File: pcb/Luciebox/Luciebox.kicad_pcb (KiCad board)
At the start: 2 copper layers, 100 x 100 mm, 91 parts, among them J1 Screw_Terminal_01x07, J2 Screw_Terminal_01x07, J3 Screw_Terminal_01x07, J4 Screw_Terminal_01x07, J5 Screw_Terminal_01x07, P1 CONN_01X01, P2 CONN_01X01, P3 CONN_01X01, P4 CONN_01X01, P5 Digital, P6 Power, P7 Digital, P8 Analog, Q1 BC558, Q2 N-Channel_Mosfet, T1 terminal_13x1, T10 terminal_8x1, T11 terminal_3x1, T2 terminal_8x1, T3 terminal_8x1, T4 terminal_8x1, T5 terminal_8x1, T6 terminal_8x1, T7 terminal_8x1, T8 terminal_8x1, T9 terminal_8x1, U1 CA56-12SRWA, U2 ULN2003A, U3 ATmega328-PU, Y1 16MHz

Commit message: fiddling with traces
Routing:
- net /0(Rx): track 149.7 -> 136.9 mm
- net /3(PWM): track 132.3 -> 142.8 mm
- net /2: track 110.3 -> 113.2 mm
- net /11(PWM-MOSI): track 72.4 -> 70.1 mm
- net /13(SCK): track 113.9 -> 115.5 mm
- net /1(Tx): track 77.6 -> 76.8 mm
- net /12(MISO): track 146.0 -> 145.2 mm

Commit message: pcb v1.0.0 looks like all done!
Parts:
- added G***: LOGO, artwork:titles_and_text, F.Cu at (54.6, 44.8)
- added G***: LOGO, artwork:sky_with_clouds_negative, F.Cu at (50.3, 49.9)
- added U4: 8X8PADS, Luciebox:64_PADS_100mil, F.Cu at (89.5, 43.5)
- moved H6 124.7 mm to (21.1, 27.1)
- moved H5 122.3 mm to (17.9, 61.2)
- moved H7 110.3 mm to (20.7, 69.4)
- moved J4 53.3 mm to (62.0, 3.92), turned to 180 degrees
- moved H8 38.3 mm to (94.1, 77.1)
- moved Q2 28.2 mm to (32.0, 18.2)
- moved R48 27.6 mm to (35.5, 14.4)
- moved R47 22.8 mm to (35.5, 11.8), turned to 180 degrees
- moved R19 18.5 mm to (75.2, 56.0), turned to 180 degrees
- moved Q1 6.78 mm to (37.1, 3.70)
- moved R1 5.04 mm to (35.5, 9.03), turned to 180 degrees
- moved R5 4.19 mm to (43.2, 30.4), turned to 90 degrees
- moved R4 1.79 mm to (53.1, 30.3)
- moved R3 0.42 mm to (57.9, 30.3)
- moved T11 0.27 mm to (2.28, 46.1)
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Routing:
- net VCC: track 293.5 -> 364.0 mm, vias 2 -> 1
- net Net-(J5-Pad2): track 24.7 -> 56.3 mm
- net /1(Tx): track 76.8 -> 104.2 mm, vias 0 -> 1
- net Net-(J4-Pad5): track 79.6 -> 102.8 mm, vias 1 -> 2
- net /3(PWM): track 142.8 -> 122.6 mm
- net GND: track 164.5 -> 182.3 mm
- net /6(PWM): track 111.1 -> 122.9 mm
- net Net-(U4-Pad25): track 0.00 -> 8.85 mm
- net Net-(U4-Pad49): track 0.00 -> 8.34 mm
- net Net-(U4-Pad33): track 0.00 -> 8.13 mm
- net Net-(U4-Pad17): track 0.00 -> 8.09 mm
- net Net-(U4-Pad41): track 0.00 -> 7.99 mm
- net +12V: track 45.9 -> 53.8 mm
- net Net-(U4-Pad10): track 0.00 -> 7.64 mm
- net Net-(J3-Pad1): track 33.5 -> 27.5 mm
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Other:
- board text added: "DAC_A0"
- board text added: "DAC_A1"
- board text added: "DAC_A2"
- board text added: "DAC_A3"
- board text added: "DAC_A4"
- board text added: "GND"
- board text added: "GND (OFF) NC"
- board text added: "GND SWITCHED"
- board text added: "INPUT (BYPASS MCU)"
- board text added: "LSB"
- board text added: "Luciebox v1.0.0 a nonkel Lode production 2019-04-01 (well... more like 2019-11)"
- board text added: "MSB"
- board text added: "OUT: 3 13 12 8 4 2 7"
- board text added: "PULL DOWN IF NC NOT AVAILABLE"
- board text added: "SWITCH"
- board text added: "VCC"
- board text added: "VCC (ON) NO"
- board text added: "Vsup"

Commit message: pcb add clouds soldermask back, create gerber files
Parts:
- added G***: LOGO, artwork:sky_with_clouds_negative_back, F.Cu at (50.2, 50.3)
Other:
- board text added: "3 13 12 8 4 2 7"
- board text removed: "INPUT (BYPASS MCU)"

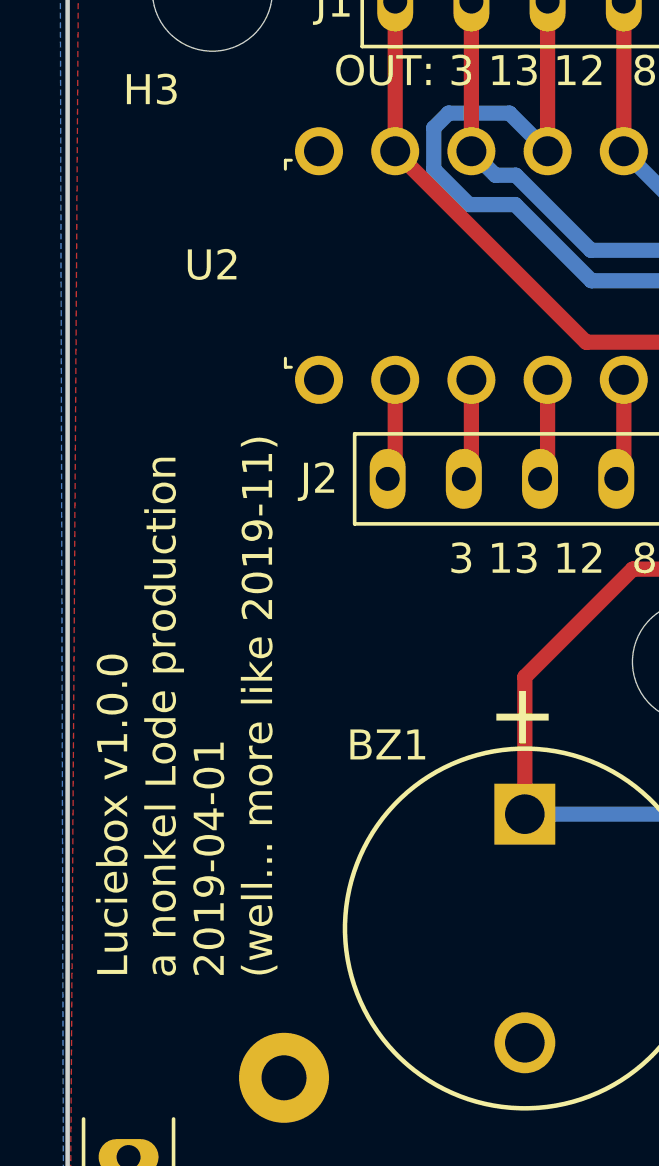
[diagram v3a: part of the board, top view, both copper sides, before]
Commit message: pcb v1.0.0 finished and ordered at jlcpcb.com
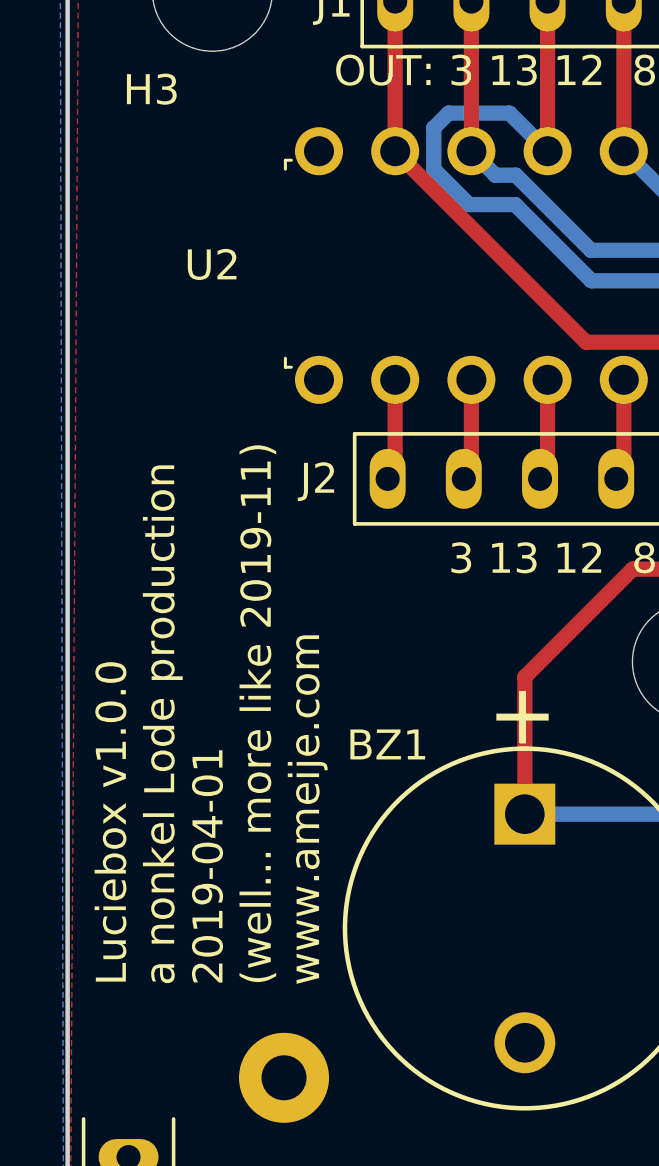
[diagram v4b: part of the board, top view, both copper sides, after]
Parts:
- added G***: LOGO, artwork:sky_clouds_negative_back, F.Cu at (50.3, 50.2)
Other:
- board text added: "Luciebox v1.0.0 a nonkel Lode production 2019-04-01 (well... more like 2019-11) www.ameije.com"
- board text removed: "Luciebox v1.0.0 a nonkel Lode production 2019-04-01 (well... more like 2019-11)"

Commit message: reload autosave, the v1.0.0 save was not actually saved. oioioi. So, now at v1.0.0 pcb!
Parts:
- removed the G*** at (50.3, 49.9)
- added G***: LOGO, artwork:sky_with_clouds_negative_adapted_silk, F.Cu at (50.0, 49.8)
- moved G*** 4.84 mm to (59.4, 45.2)

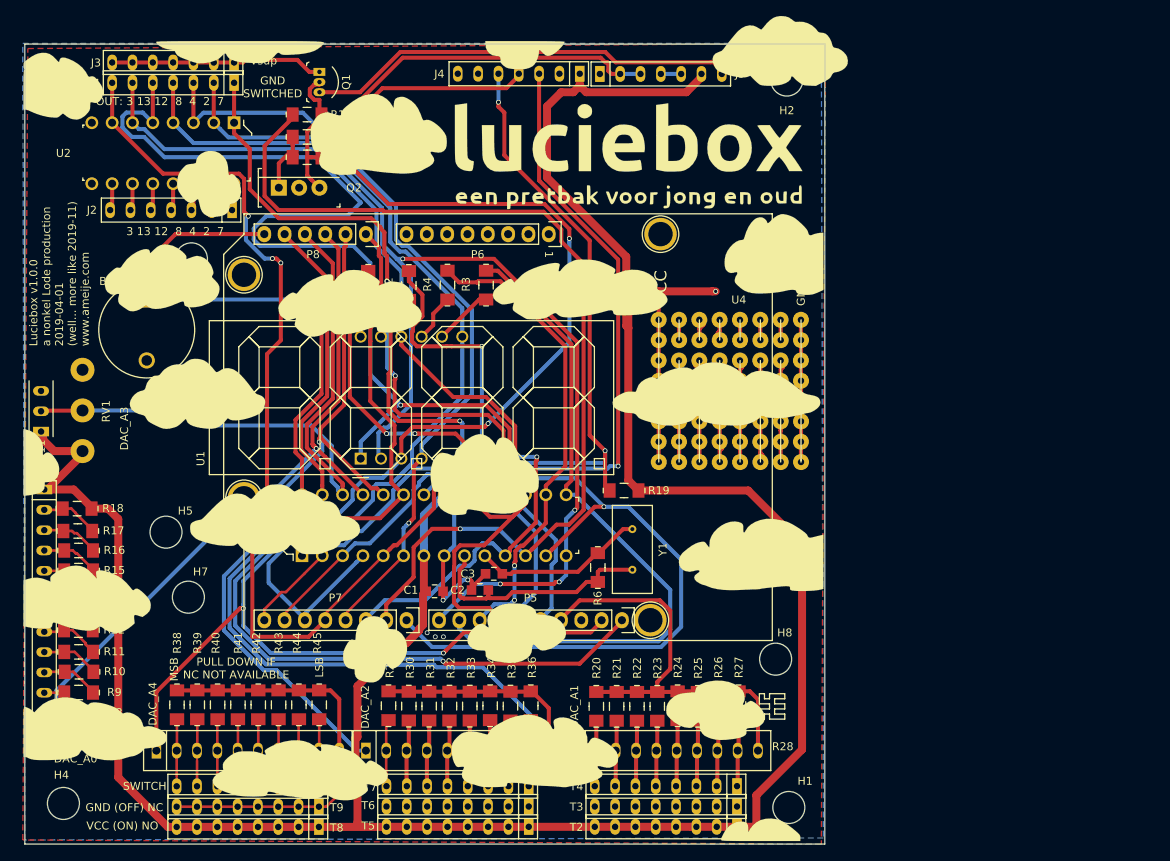
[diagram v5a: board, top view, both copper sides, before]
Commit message: buttons and selector switch debugging. Starting to change pcb schematic for v2.0 board
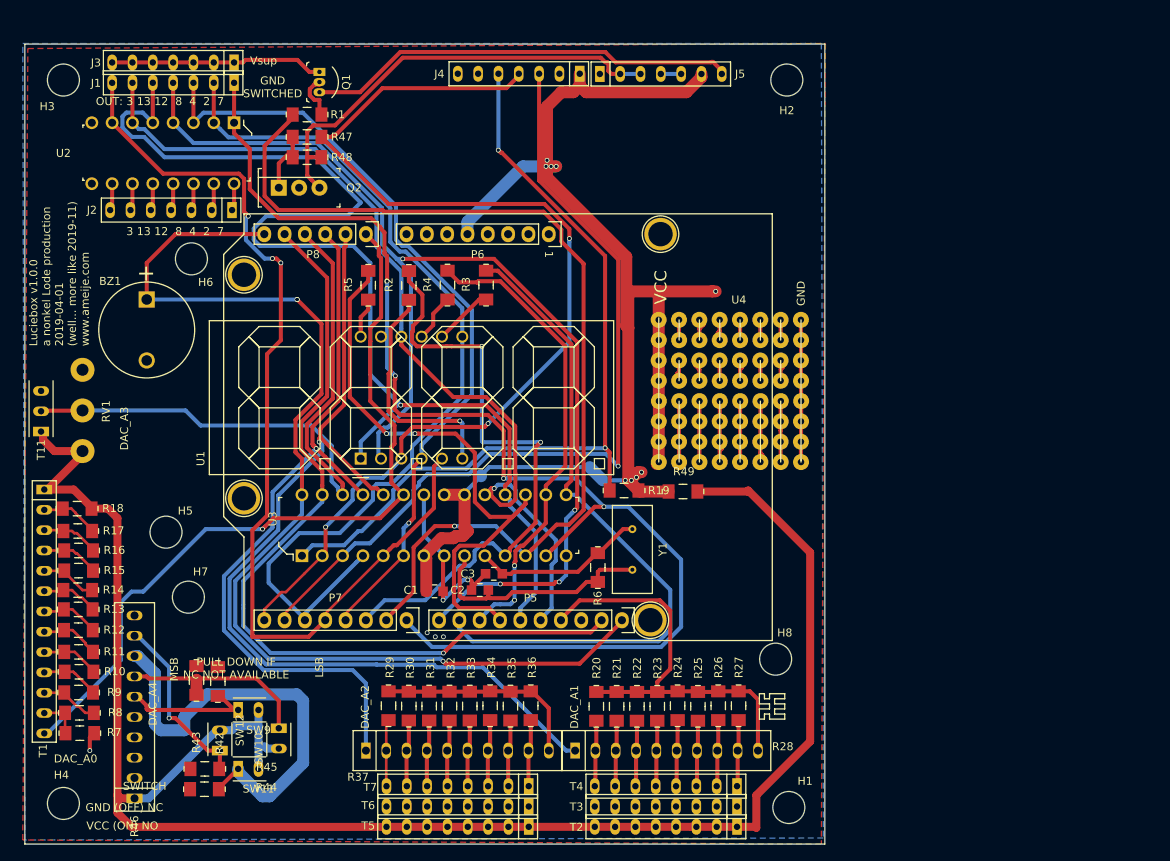
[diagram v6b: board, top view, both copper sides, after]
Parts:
- removed G***: LOGO, artwork:sky_with_clouds_negative_adapted_silk
- removed G***: LOGO, artwork:sky_clouds_negative_back
- removed G***: LOGO, artwork:sky_with_clouds_negative_back
- removed G***: LOGO, artwork:titles_and_text
- removed R38, R39, R40, R41: R_Small, Luciebox:1206
- removed T10, T8, T9: terminal_8x1, Luciebox:Terminal_8x1_100mil
- added R49: 10K, Luciebox:1206, F.Cu at (82.5, 56.1)
- added SW10: Switch_tilt, Luciebox:Terminal_2x1_100mil, F.Cu at (32.0, 88.3)
- added SW11: Switch_tilt, Luciebox:Terminal_2x1_100mil, F.Cu at (29.5, 90.8)
- added SW12: Switch_tilt, Luciebox:Terminal_2x1_100mil, F.Cu at (24.6, 86.0)
- added SW9: Switch_tilt, Luciebox:Terminal_2x1_100mil, F.Cu at (29.5, 83.5)
- moved R45 16.4 mm to (22.7, 90.8), turned to 0 degrees
- moved R44 15.8 mm to (22.7, 93.4), turned to 0 degrees
- moved R46 15.2 mm to (14.0, 83.1), turned to 90 degrees
- moved R43 10.7 mm to (21.7, 79.8), turned to 270 degrees
- moved R42 5.83 mm to (24.4, 79.9), turned to 270 degrees
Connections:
- P6 pad 5: +5V -> VCC
- R18 pad 1: VCC -> VCC_minimalCurrent
- R42 pad 1: Net-(R42-Pad1) -> GND
- R42 pad 2: GND -> Net-(R42-Pad2)
- R43 pad 1: Net-(R43-Pad1) -> GND
- R43 pad 2: GND -> Net-(R43-Pad2)
- R44 pad 1: Net-(R44-Pad1) -> GND
- R44 pad 2: GND -> Net-(R44-Pad2)
- R45 pad 1: Net-(R45-Pad1) -> GND
- R45 pad 2: GND -> Net-(R45-Pad2)
- R46 pad 1: /A4(SDA) -> VCC_minimalCurrent
- R46 pad 6: Net-(R42-Pad1) -> Net-(R42-Pad2)
- R46 pad 7: Net-(R43-Pad1) -> Net-(R43-Pad2)
- R46 pad 8: Net-(R44-Pad1) -> Net-(R44-Pad2)
- R46 pad 9: Net-(R45-Pad1) -> Net-(R45-Pad2)
- RV1 pad 1: VCC -> VCC_minimalCurrent
- T1 pad 1: VCC -> VCC_minimalCurrent
- T11 pad 1: VCC -> VCC_minimalCurrent
- T2 pad 1: VCC -> VCC_minimalCurrent
- T2 pad 2: VCC -> VCC_minimalCurrent
- T2 pad 3: VCC -> VCC_minimalCurrent
- T2 pad 4: VCC -> VCC_minimalCurrent
- T2 pad 5: VCC -> VCC_minimalCurrent
- T2 pad 6: VCC -> VCC_minimalCurrent
- T2 pad 7: VCC -> VCC_minimalCurrent
- T2 pad 8: VCC -> VCC_minimalCurrent
- T5 pad 1: VCC -> VCC_minimalCurrent
- T5 pad 2: VCC -> VCC_minimalCurrent
- T5 pad 3: VCC -> VCC_minimalCurrent
- T5 pad 4: VCC -> VCC_minimalCurrent
- T5 pad 5: VCC -> VCC_minimalCurrent
- T5 pad 6: VCC -> VCC_minimalCurrent
- T5 pad 7: VCC -> VCC_minimalCurrent
- T5 pad 8: VCC -> VCC_minimalCurrent
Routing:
- net VCC_minimalCurrent: track 0.00 -> 228.6 mm
- net VCC: track 364.0 -> 180.2 mm, vias 1 -> 9
- net GND: track 182.3 -> 124.1 mm
- net Net-(R44-Pad2): track 0.00 -> 55.0 mm
- net Net-(R43-Pad2): track 0.00 -> 24.6 mm
- net Net-(R45-Pad2): track 0.00 -> 22.7 mm, vias 0 -> 1
- net /A4(SDA): track 128.2 -> 105.7 mm, vias 2 -> 1
- net Net-(R42-Pad2): track 0.00 -> 16.5 mm
- net Net-(R46-Pad2): track 8.40 -> 0.00 mm
- net Net-(R46-Pad3): track 8.40 -> 0.00 mm
- net Net-(R45-Pad1): track 8.40 -> 0.00 mm
- net Net-(R46-Pad5): track 8.40 -> 0.00 mm
- net Net-(R46-Pad4): track 8.40 -> 0.00 mm
- net Net-(R43-Pad1): track 8.40 -> 0.00 mm
- net Net-(R44-Pad1): track 8.40 -> 0.00 mm
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
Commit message: changes in pcb v2.0
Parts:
- added D1: D_Schottky, Luciebox:smd_throughhole_2_pins, F.Cu at (86.3, 23.0)
- added J7: USB_B_Mini, Luciebox:usb_mini_Molex-0548190519, F.Cu at (100.2, 18.1)
- added T8: terminal_3x1, Luciebox:Terminal_3x1_100mil, F.Cu at (97.1, 28.7)
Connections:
- R46 pad 1: VCC_minimalCurrent -> Net-(R46-Pad1)
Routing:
- net Net-(J7-Pad3): track 0.00 -> 17.1 mm
- net Net-(J7-Pad2): track 0.00 -> 15.7 mm
- net Net-(J7-Pad4): track 0.00 -> 9.23 mm
- net Net-(D1-Pad2): track 0.00 -> 8.18 mm
- net VCC: track 180.2 -> 184.6 mm

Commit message: progressive change towards v2.0
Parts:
- R1, R10, R11, R12, R13, R14, R15, R16, R17, R18, R19, R2, R20, R21, R22, R23, R24, R25, R26, R27, R29, R3, R30, R31, R32, R33, R34, R35, R36, R4, R42, R43, R44, R45, R47, R48, R49, R5, R6, R7, R8, R9: footprint Luciebox:1206 -> Luciebox:1206_0805
- moved H6 19.3 mm to (16.8, 45.9)
- moved SW10 1.27 mm to (33.3, 88.3)
- moved R42 1.27 mm to (25.6, 79.9)
- moved R44 1.27 mm to (24.0, 93.4)
- moved R45 1.27 mm to (24.0, 90.8)
- moved SW11 1.27 mm to (30.7, 90.8)
- moved SW12 1.27 mm to (25.9, 86.0)
- moved SW9 1.27 mm to (30.7, 83.5)
- moved R43 0.13 mm to (21.6, 79.8)
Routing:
- net Net-(R43-Pad2): track 24.6 -> 36.1 mm
- net VCC: track 184.6 -> 178.1 mm
- net VCC_minimalCurrent: track 228.6 -> 232.9 mm, vias 0 -> 3
- net /A5(SCL): track 139.4 -> 136.7 mm
- net Net-(R45-Pad2): track 22.7 -> 23.9 mm
- net Net-(R42-Pad2): track 16.5 -> 15.6 mm
- net /1(Tx): track 105.5 -> 106.1 mm
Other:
- board text added: "AUX Power Supply"
- board text added: "BAT +"
- board text added: "BAT -"
- board text added: "Luciebox v2.0.0 a nonkel Lode production 2020-04-02. Blijde herinnering aan 1 jaar Lucie(box). www.ameije.com"
- board text added: "ON-Switch"
- board text added: "RX"
- board text added: "Reset"
- board text added: "TX"
- board text added: "Touch Power ON"
- board text removed: "Luciebox v1.0.0 a nonkel Lode production 2019-04-01 (well... more like 2019-11) www.ameije.com"
